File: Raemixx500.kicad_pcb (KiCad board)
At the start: 2 copper layers, 365.8 x 254 mm, 372 parts, among them CN1 LEFT_JOY, CN10 COMPOSITE, CN11 INTERNAL_FLOPPY, CN12 FLOPPY_POWER, CN13 KEYBOARD, CN14 IDE_POWER, CN15 IDE_I/F, CN2 RIGHT_JOY, CN3 RIGHT, CN4 LEFT, CN5 EXTFLOPPY_DB23F, CN6 SERIAL_DB25M, CN7 PARALLEL_DB25F, CN8 POWER, CN9 VIDEO_DB23M, J90 DRIVE_SWITCHER, J91 Dispatcher_3to1, J92 Dispatcher_3to1, J93 Dispatcher_3to1, J99 HD_ACT, P1 EXPANSION BUS, P9 TRAPDOOR, Q301 2N3906, Q321 MPF102 / J113, Q331 MPF102 / J113, Q501 2N3904, Q502 2N3906, Q503 2N3906, Q504 2N3904, Q711 2N3904, Q921 MMBFJ113, Q931 MMBFJ113, U1 68000D, U10 74LS244, U11 74LS373, U12 74LS244, U13 74LS373, U14 LF347, U15 74LS157, U16 SIMM, U17 74F08, U18 74F74, U19 74F00, U2 FAT_AGNUS_8375, U3 PAULA, U32 74F139, U33 74F258, U34 74F244, U35 74F244, U36 74LS05, U37 74LS32, U38 MC1488, U39 MC1489, U4 DENISE, U40 74HCT245, U41 74HCT245, U42 NE555, U5 GARY_5719, U6 ROM, U7 VIA_8520, U8 VIA_8520, U9 MSM6242B, U94 74HCT14, X1 XTAL, Y9 32.768kHz

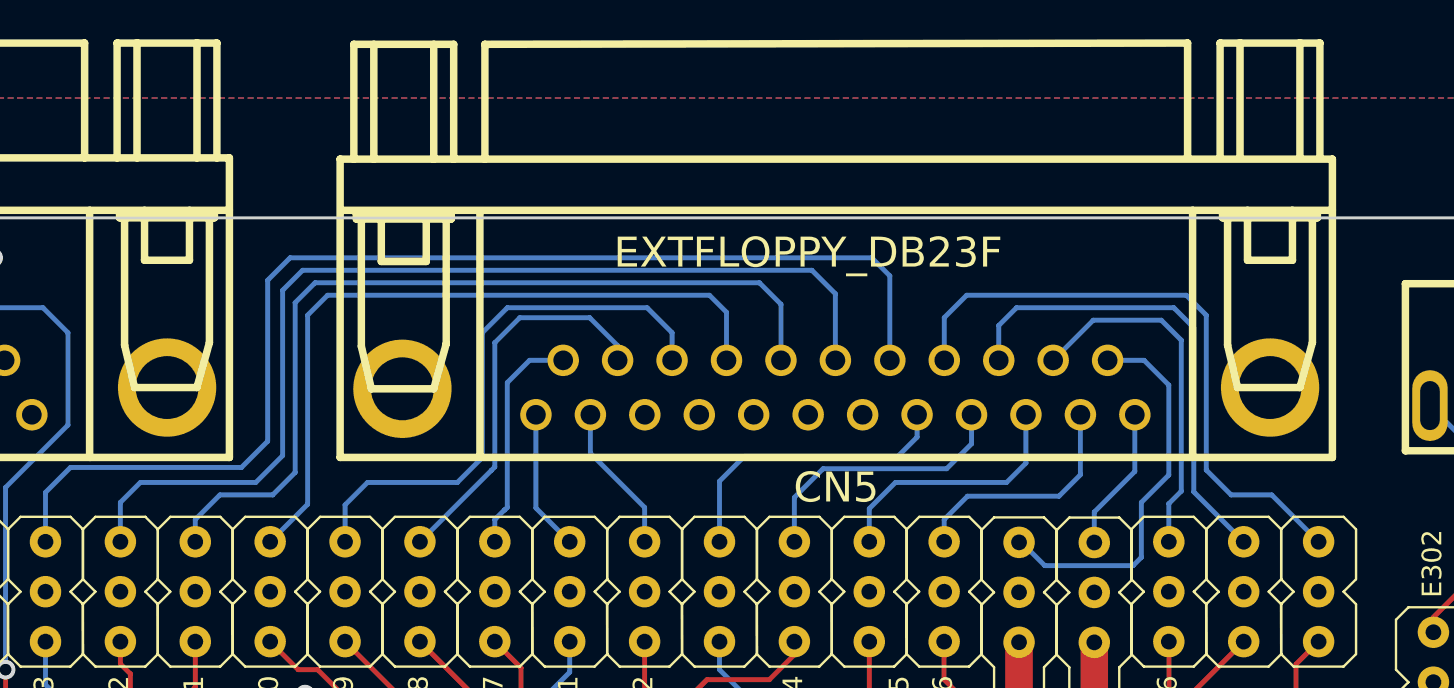
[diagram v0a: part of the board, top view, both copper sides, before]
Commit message: moved floppy connector 0.3mm away from audio output connectors
bumped version on schematics and PCB to V3.1
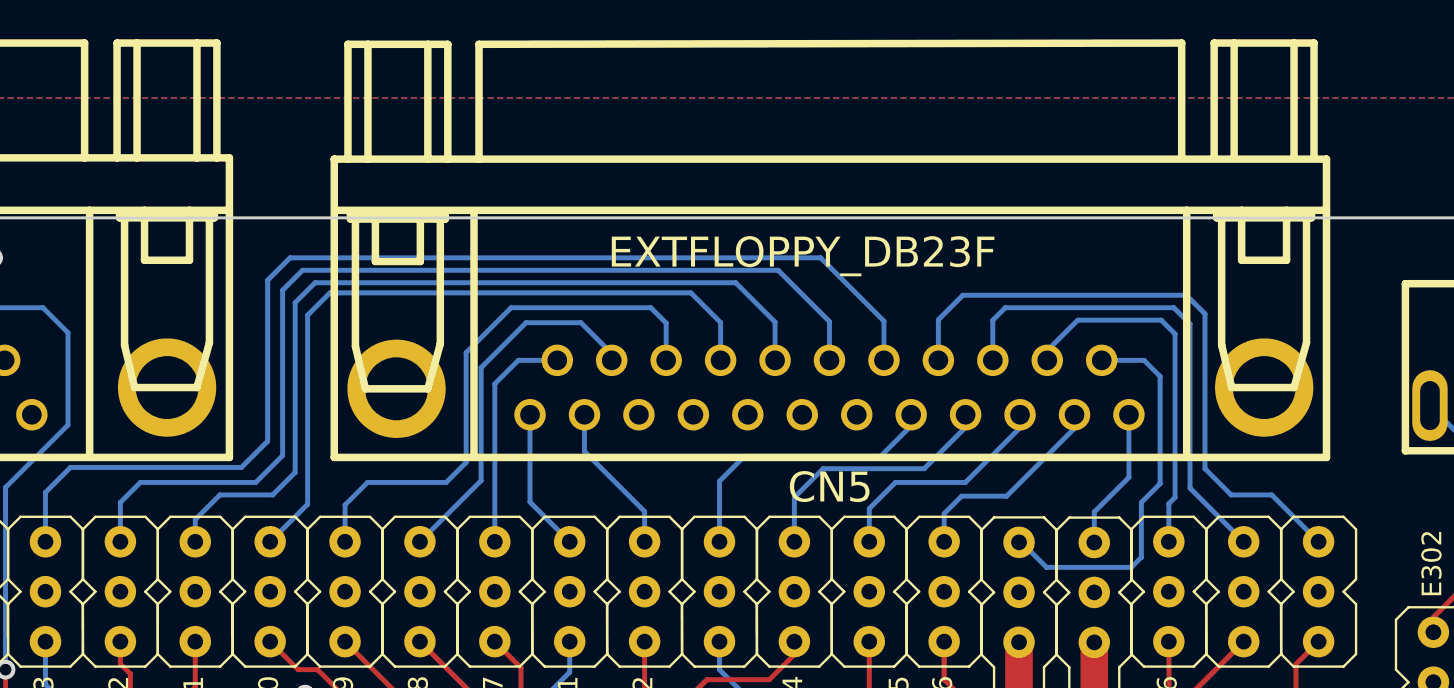
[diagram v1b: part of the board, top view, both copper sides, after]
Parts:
- moved CN5 0.30 mm to (264.8, 25.5)
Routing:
- net Net-(CN5-P19): track 59.9 -> 58.2 mm
- net Net-(CN5-Pad11): track 12.1 -> 10.5 mm
- net Net-(CN5-Pad10): track 13.1 -> 11.7 mm
- net Net-(CN5-P18): track 52.1 -> 51.0 mm
- net Net-(CN5-P14): track 19.8 -> 18.7 mm
- net Net-(CN5-P17): track 44.3 -> 43.5 mm
- net Net-(CN5-Pad9): track 13.9 -> 13.1 mm
- net Net-(CN5-Pad8): track 15.2 -> 14.6 mm
- net Net-(CN5-P16): track 36.9 -> 36.3 mm
